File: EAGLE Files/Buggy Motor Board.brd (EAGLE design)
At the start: 100 x 80 mm, 48 parts, among them CON0 M025MM, CON1 M025MM, IC4 4050D, IC5 LP298XS, U1 MCP2551, X1 MICROSD, X2 5566-24, X3 5566-24, Y2 16MHZ

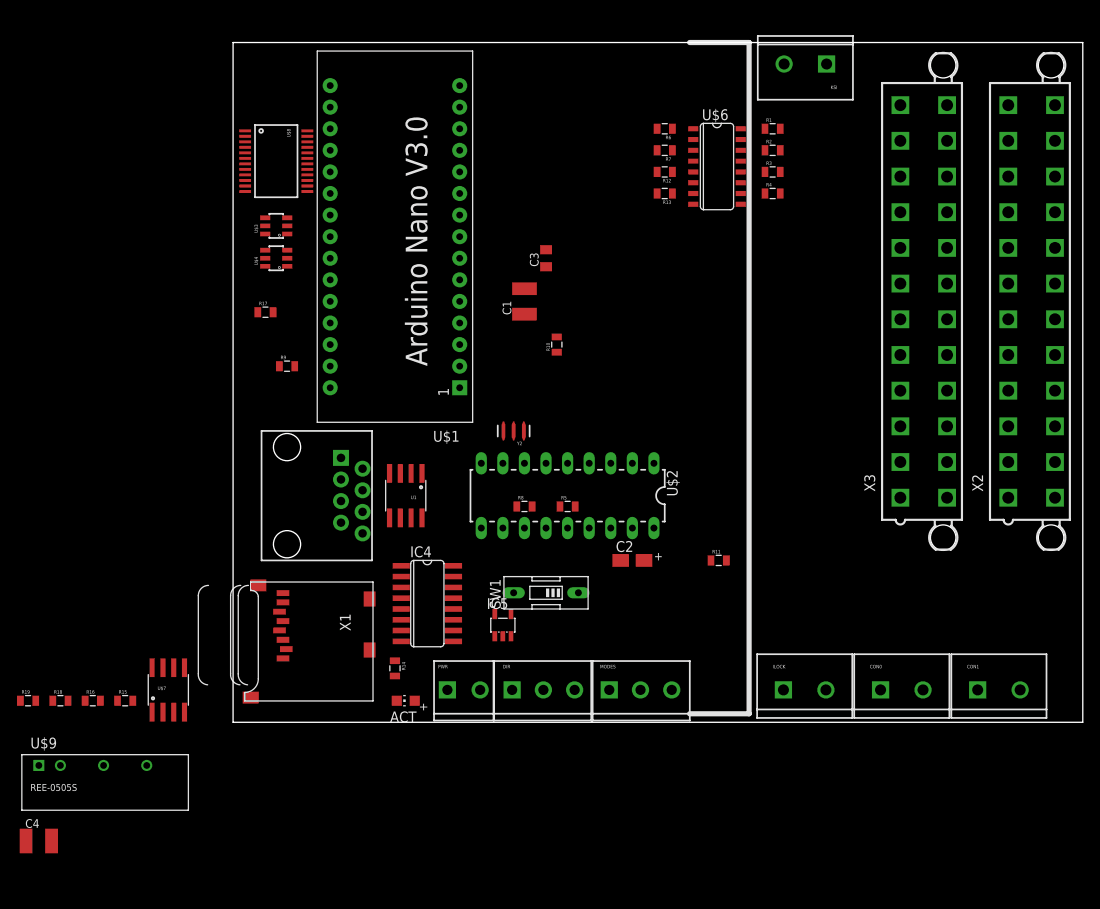
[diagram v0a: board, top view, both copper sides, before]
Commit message: Power consumption, analog input connectors
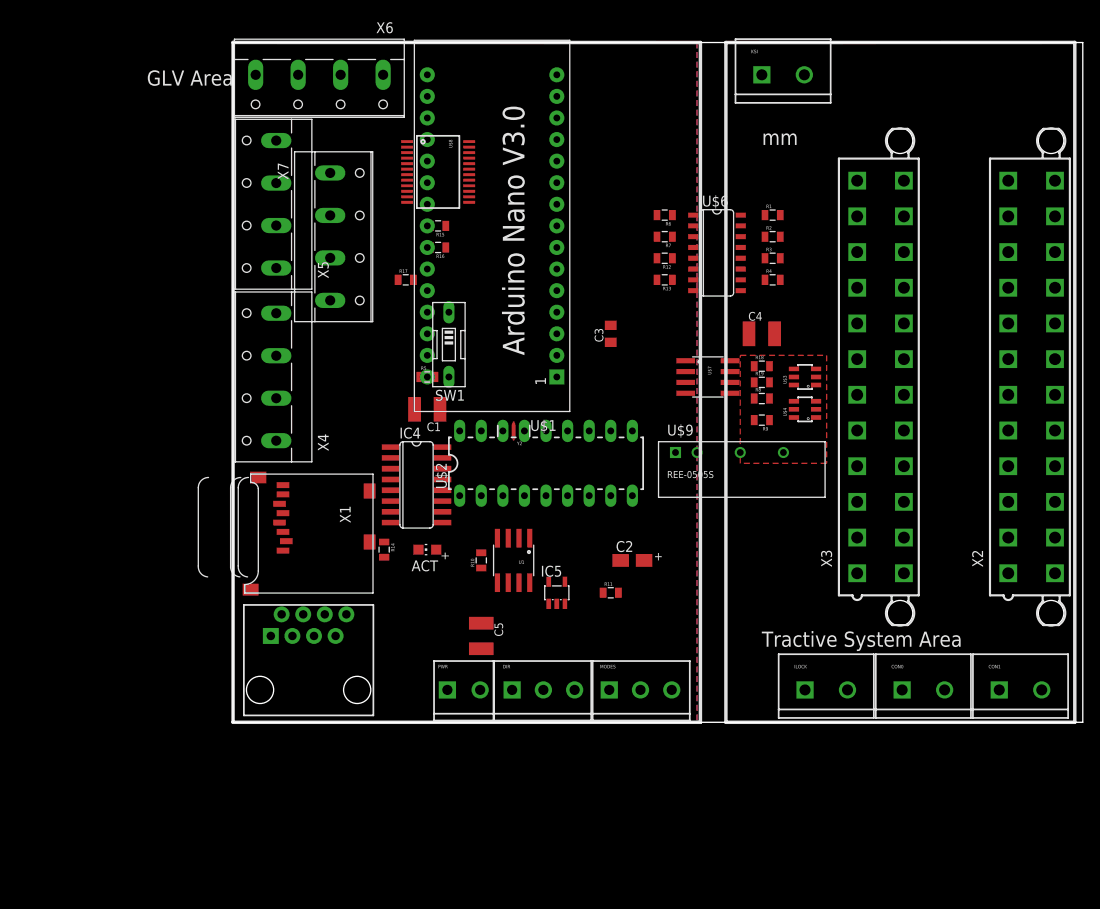
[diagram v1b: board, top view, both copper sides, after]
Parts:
- added C5: (no value), rcl:C1210K
- added X4, X5, X6, X7: (no value), con-wago-500:W237-4
- R15, R16, R18, R19: value (none) -> 4.7k
- moved C4 103.9 mm to (62.2, 45.7)
- moved R19 94.1 mm to (62.2, 40.0)
- moved R18 91.5 mm to (62.2, 41.9)
- moved U$9 83.5 mm to (52.1, 31.8)
- moved U$7 73.4 mm to (55.9, 40.6), turned to 270 degrees
- moved R16 67.1 mm to (24.1, 55.9), turned to 180 degrees
- moved R15 66.9 mm to (24.1, 58.4), turned to 180 degrees
- moved U$3 64.7 mm to (67.3, 40.6)
- moved U$4 64.7 mm to (67.3, 36.8)
- moved R9 56.2 mm to (62.2, 35.6), turned to 180 degrees
- moved SW1 31.4 mm to (25.4, 44.5), turned to 180 degrees
- moved R8 30.7 mm to (62.2, 38.1)
- moved R10 26.9 mm to (29.2, 19.1)
- moved U$5 23.0 mm to (8.89, 3.81), turned to 0 degrees
- moved R5 22.5 mm to (22.9, 40.6)
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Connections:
- net +5V: now also C5.1
- net CHAN0: now also X4.1
- net CHAN1: now also X4.2
- net CHAN10: now also X6.3
- net CHAN11: now also X6.4
- net CHAN12: now also X7.1
- net CHAN13: now also X7.2
- net CHAN14: now also X7.3
- net CHAN15: now also X7.4
- net CHAN2: now also X4.3
- net CHAN3: now also X4.4
- net CHAN4: now also X5.1
- net CHAN5: now also X5.2
- net CHAN6: now also X5.3
- net CHAN7: now also X5.4
- net CHAN8: now also X6.1
- net CHAN9: now also X6.2
- net GND: now also C5.2, U$5.6; no longer U$5.1, U$5.2, U$5.3, U$5.4
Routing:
- added copper zone on layer 1, net +5V
- added copper zone on layer 1, net +5V/1
- added copper zone on layer 16, net GND
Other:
- board text added: "GLV Area"
- board text added: "Tractive System Area"
- board text added: "mm"

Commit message: Microfit connector
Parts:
- removed X4, X5, X6, X7: (no value), con-wago-500:W237-4
- added U$10: WM9300, Wetmelon-Connectors:WM9300
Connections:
- net CHAN0: no longer X4.1
- net CHAN1: no longer X4.2
- net CHAN10: no longer X6.3
- net CHAN11: no longer X6.4
- net CHAN12: no longer X7.1
- net CHAN13: no longer X7.2
- net CHAN14: no longer X7.3
- net CHAN15: no longer X7.4
- net CHAN2: no longer X4.3
- net CHAN3: no longer X4.4
- net CHAN4: no longer X5.1
- net CHAN5: no longer X5.2
- net CHAN6: no longer X5.3
- net CHAN7: no longer X5.4
- net CHAN8: no longer X6.1
- net CHAN9: no longer X6.2
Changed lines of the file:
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@@
 <element name="C4" library="rcl" package="C1210K" value="" x="62.23" y="45.72"/>
 <element name="C5" library="rcl" package="C1210K" value="" x="29.21" y="10.16" rot="R270"/>
-<element name="X4" library="con-wago-500" package="W237-4" value="" x="3.81" y="40.64" rot="R90">
-<attribute name="OC_NEWARK" value="unknown" x="3.81" y="40.64" size="1.778" layer="27" rot="R90" display="off"/>
-<attribute name="MPN" value="" x="3.81" y="40.64" size="1.778" layer="27" rot="R90" display="off"/>
-<attribute name="MF" value="" x="3.81" y="40.64" size="1.778" layer="27" rot="R90" display="off"/>
-<attribute name="OC_FARNELL" value="unknown" x="3.81" y="40.64" size="1.778" layer="27" rot="R90" display="off"/>
-</element>
-<element name="X5" library="con-wago-500" package="W237-4" value="" x="3.81" y="60.96" rot="R90">
-<attribute name="OC_NEWARK" value="unknown" x="3.81" y="60.96" size="1.778" layer="27" rot="R90" display="off"/>
-<attribute name="MPN" value="" x="3.81" y="60.96" size="1.778" layer="27" rot="R90" display="off"/>
-<attribute name="MF" value="" x="3.81" y="60.96" size="1.778" layer="27" rot="R90" display="off"/>
-<attribute name="OC_FARNELL" value="unknown" x="3.81" y="60.96" size="1.778" layer="27" rot="R90" display="off"/>
-</element>
-<element name="X6" library="con-wago-500" package="W237-4" value="" x="10.16" y="74.93" rot="R180">
-<attribute name="OC_NEWARK" value="unknown" x="10.16" y="74.93" size="1.778" layer="27" rot="R180" display="off"/>
-<attribute name="MPN" value="" x="10.16" y="74.93" size="1.778" layer="27" rot="R180" display="off"/>
-<attribute name="MF" value="" x="10.16" y="74.93" size="1.778" layer="27" rot="R180" display="off"/>
-<attribute name="OC_FARNELL" value="unknown" x="10.16" y="74.93" size="1.778" layer="27" rot="R180" display="off"/>
-</element>
-<element name="X7" library="con-wago-500" package="W237-4" value="" x="12.7" y="57.15" rot="R270">
-<attribute name="OC_NEWARK" value="unknown" x="12.7" y="57.15" size="1.778" layer="27" rot="R270" display="off"/>
-<attribute name="MPN" value="" x="12.7" y="57.15" size="1.778" layer="27" rot="R270" display="off"/>
-<attribute name="MF" value="" x="12.7" y="57.15" size="1.778" layer="27" rot="R270" display="off"/>
-<attribute name="OC_FARNELL" value="unknown" x="12.7" y="57.15" size="1.778" layer="27" rot="R270" display="off"/>
-</element>
+<element name="U$10" library="Wetmelon-Connectors" package="WM9300" value="WM9300" x="3.81" y="-13.97"/>
 </elements>
 <signals>
@@
 <signal name="CHAN0">
 <contactref element="U$8" pad="9"/>
-<contactref element="X4" pad="1"/>
-<wire x1="5.08" y1="33.14" x2="20.474" y2="63.145" width="0" layer="19" extent="1-1"/>
 </signal>
 <signal name="CHAN1">
 <contactref element="U$8" pad="8"/>
-<contactref element="X4" pad="2"/>
-<wire x1="5.08" y1="38.14" x2="20.474" y2="63.795" width="0" layer="19" extent="1-1"/>
 </signal>
 <signal name="CHAN2">
 <contactref element="U$8" pad="7"/>
-<contactref element="X4" pad="3"/>
-<wire x1="5.08" y1="43.14" x2="20.474" y2="64.445" width="0" layer="19" extent="1-1"/>
 </signal>
 <signal name="CHAN3">
 <contactref element="U$8" pad="6"/>
-<contactref element="X4" pad="4"/>
-<wire x1="5.08" y1="48.14" x2="20.474" y2="65.095" width="0" layer="19" extent="1-1"/>
 </signal>
 <signal name="CHAN4">
 <contactref element="U$8" pad="5"/>
-<contactref element="X5" pad="1"/>
-<wire x1="5.08" y1="53.46" x2="20.474" y2="65.745" width="0" layer="19" extent="1-1"/>
 </signal>
 <signal name="CHAN5">
 <contactref element="U$8" pad="4"/>
-<contactref element="X5" pad="2"/>
-<wire x1="5.08" y1="58.46" x2="20.474" y2="66.395" width="0" layer="19" extent="1-1"/>
 </signal>
 <signal name="CHAN6">
 <contactref element="U$8" pad="3"/>
-<contactref element="X5" pad="3"/>
-<wire x1="5.08" y1="63.46" x2="20.474" y2="67.045" width="0" layer="19" extent="1-1"/>
 </signal>
 <signal name="CHAN7">
 <contactref element="U$8" pad="2"/>
-<contactref element="X5" pad="4"/>
-<wire x1="5.08" y1="68.46" x2="20.474" y2="67.695" width="0" layer="19" extent="1-1"/>
 </signal>
 <signal name="CHAN8">
 <contactref element="U$8" pad="23"/>
-<contactref element="X6" pad="1"/>
-<wire x1="17.66" y1="76.2" x2="27.786" y2="67.695" width="0" layer="19" extent="1-1"/>
 </signal>
 <signal name="CHAN9">
 <contactref element="U$8" pad="22"/>
-<contactref element="X6" pad="2"/>
-<wire x1="12.66" y1="76.2" x2="27.786" y2="67.045" width="0" layer="19" extent="1-1"/>
 </signal>
 <signal name="CHAN10">
 <contactref element="U$8" pad="21"/>
-<contactref element="X6" pad="3"/>
-<wire x1="7.66" y1="76.2" x2="27.786" y2="66.395" width="0" layer="19" extent="1-1"/>
 </signal>
 <signal name="CHAN11">
 <contactref element="U$8" pad="20"/>
-<contactref element="X6" pad="4"/>
-<wire x1="2.66" y1="76.2" x2="27.786" y2="65.745" width="0" layer="19" extent="1-1"/>
 </signal>
 <signal name="CHAN12">
 <contactref element="U$8" pad="19"/>
-<contactref element="X7" pad="1"/>
-<wire x1="11.43" y1="64.65" x2="27.786" y2="65.095" width="0" layer="19" extent="1-1"/>
 </signal>
 <signal name="CHAN13">
 <contactref element="U$8" pad="18"/>
-<contactref element="X7" pad="2"/>
-<wire x1="11.43" y1="59.65" x2="27.786" y2="64.445" width="0" layer="19" extent="1-1"/>
 </signal>
 <signal name="CHAN14">
 <contactref element="U$8" pad="17"/>
-<contactref element="X7" pad="3"/>
-<wire x1="11.43" y1="54.65" x2="27.786" y2="63.795" width="0" layer="19" extent="1-1"/>
 </signal>
 <signal name="CHAN15">
 <contactref element="U$8" pad="16"/>
-<contactref element="X7" pad="4"/>
-<wire x1="11.43" y1="49.65" x2="27.786" y2="63.145" width="0" layer="19" extent="1-1"/>
 </signal>
 <signal name="N$12">
